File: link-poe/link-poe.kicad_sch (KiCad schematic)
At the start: 27 parts, among them J101 2x05_Horizontal, J102 NE8FAH, J103 JAE_DX07S016JA3, J104 2x05_Horizontal, J105 NE8FAH, J106 WAGO-2065, J107 WAGO-2065, J108 WAGO-2065, J109 WAGO-2065

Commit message: Refresh
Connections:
- net +24V-Supply renamed +24V-Link
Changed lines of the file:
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@@
 		)
 	)
-	(label "+24V-Supply"
+	(label "+24V-Link"
 		(at 78.74 52.07 180)
 		(effects
@@
 		)
 	)
-	(label "+24V-Supply"
+	(label "+24V-Link"
 		(at 46.99 26.67 0)
 		(effects
@@
 		)
 	)
-	(label "+24V-Supply"
+	(label "+24V-Link"
 		(at 78.74 90.17 180)
 		(effects
@@
 		)
 	)
-	(label "+24V-Supply"
+	(label "+24V-Link"
 		(at 30.48 158.75 0)
 		(effects

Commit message: Update
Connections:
- net Earth renamed USB-Shield
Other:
- note added: "PoE Passive +24V IEEE 802.3af Mode B"
- note added: "RS-422 3MHz"
- note added: "The cables used to connect the device and the power adapter reverse the order of the wires."
- note added: "V2 Link – PoE"
- note removed: "The cables connecting the device and the power adapter reverse the order of the wires. So these connectors are different from the otherwise identical connectors at the device."
- note removed: "V2 Link – PoE (Mode B)"
- title: V2 Link PoE (Mode B) -> V2 Link PoE
- moved on the sheet: C101, J101, J102, J103, J104, J105, J106, J107, J108, J109, R101, R102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

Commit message: Update usb + link-poe
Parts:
- C101: footprint Capacitor_SMD:C_0603_1608Metric -> V2_Capacitor_SMD:C_0603; symbol Device:C_Small -> V2_Device:C_0603_0u1; Mouser (none) -> 810-CGA3E2X7R1H104MA
- FID101, FID102, FID103: value Fiducial -> Fiducial_Paste
- ICON102: footprint V2_Artwork:Logo_Tiny -> V2_Artwork:Logo_Small
- INFO102: value ORDER-NUMBER -> Order_Number
- J101, J104: Mouser (none) -> 649-200211120001T4LF
- J102, J105: Mouser (none) -> 568-NE8FAH
- J103: value JAE_DX07S016JA3 -> DX07S016JA3; Mouser (none) -> 656-DX07S016JA3R1500
- J106, J107, J108, J109: value WAGO-2065 -> Conn_01x01
- R101, R102: footprint Resistor_SMD:R_0603_1608Metric -> V2_Resistor_SMD:R_0603; symbol Device:R_Small -> V2_Device:R_0603_5k1; Mouser (none) -> 71-CRCW06035K10FKEAC
- TVS101: value SMAJ36CA -> SMBJ36CA; footprint Diode_SMD:D_SMA -> V2_Diode_SMD:D_SMB; symbol V2_Diode:SMAJ36CA -> V2_Diode:SMBJ36CA; Mouser (none) -> 652-SMBJ36CA-Q
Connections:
- net USB-Shield renamed Earth

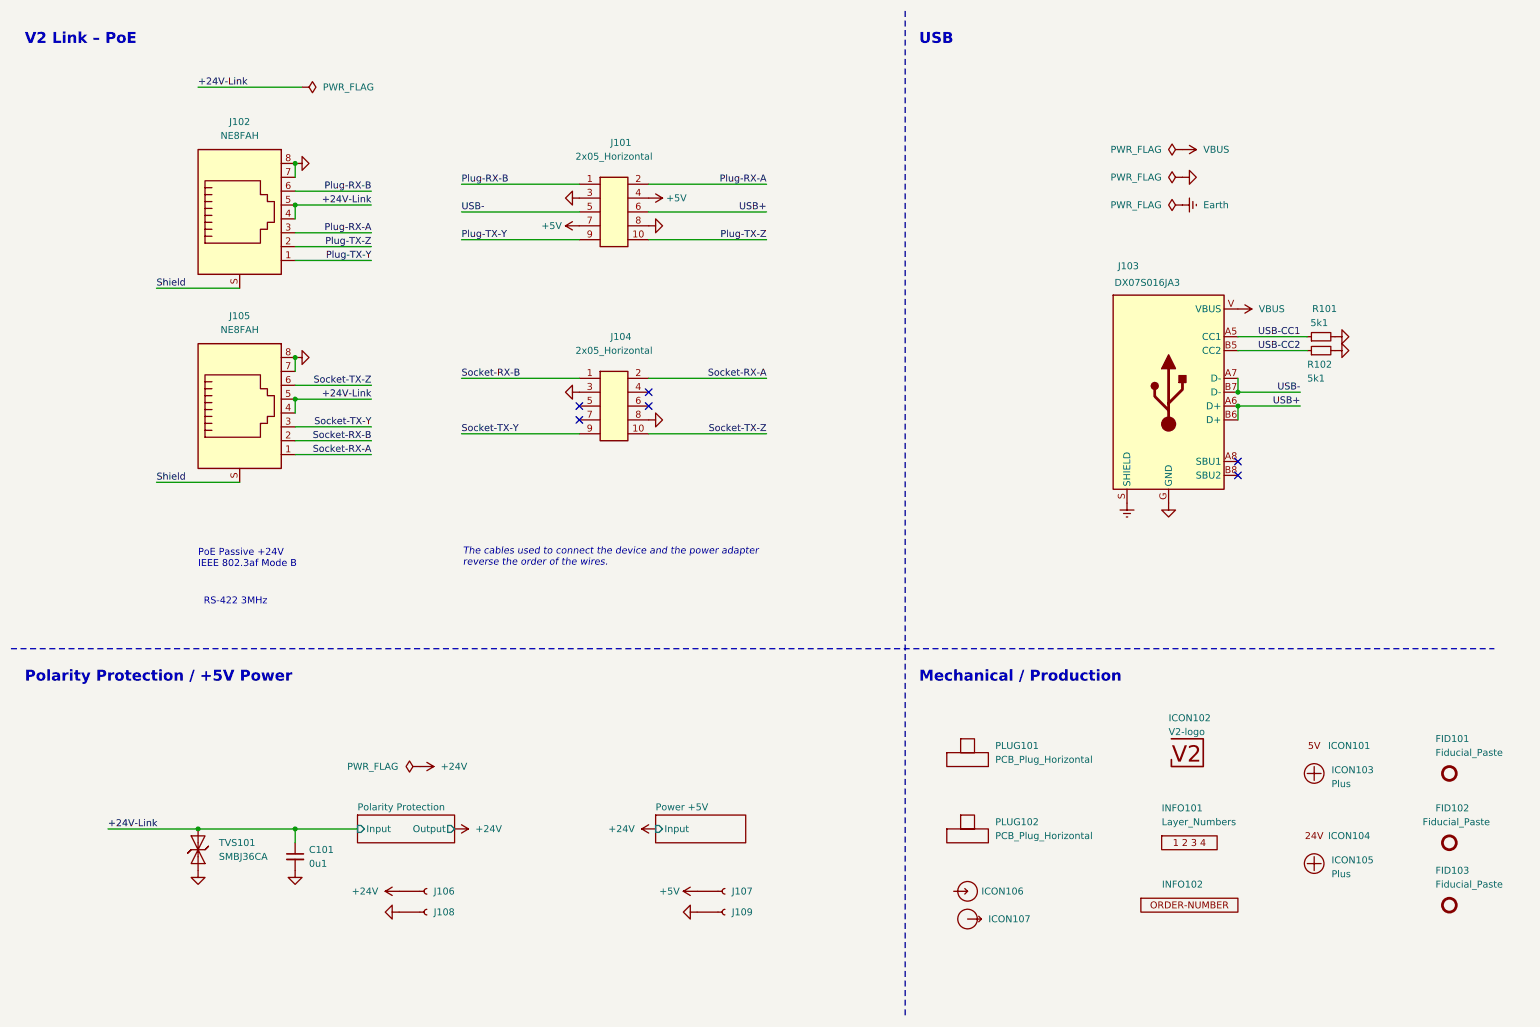
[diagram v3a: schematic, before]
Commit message: Update power symbols
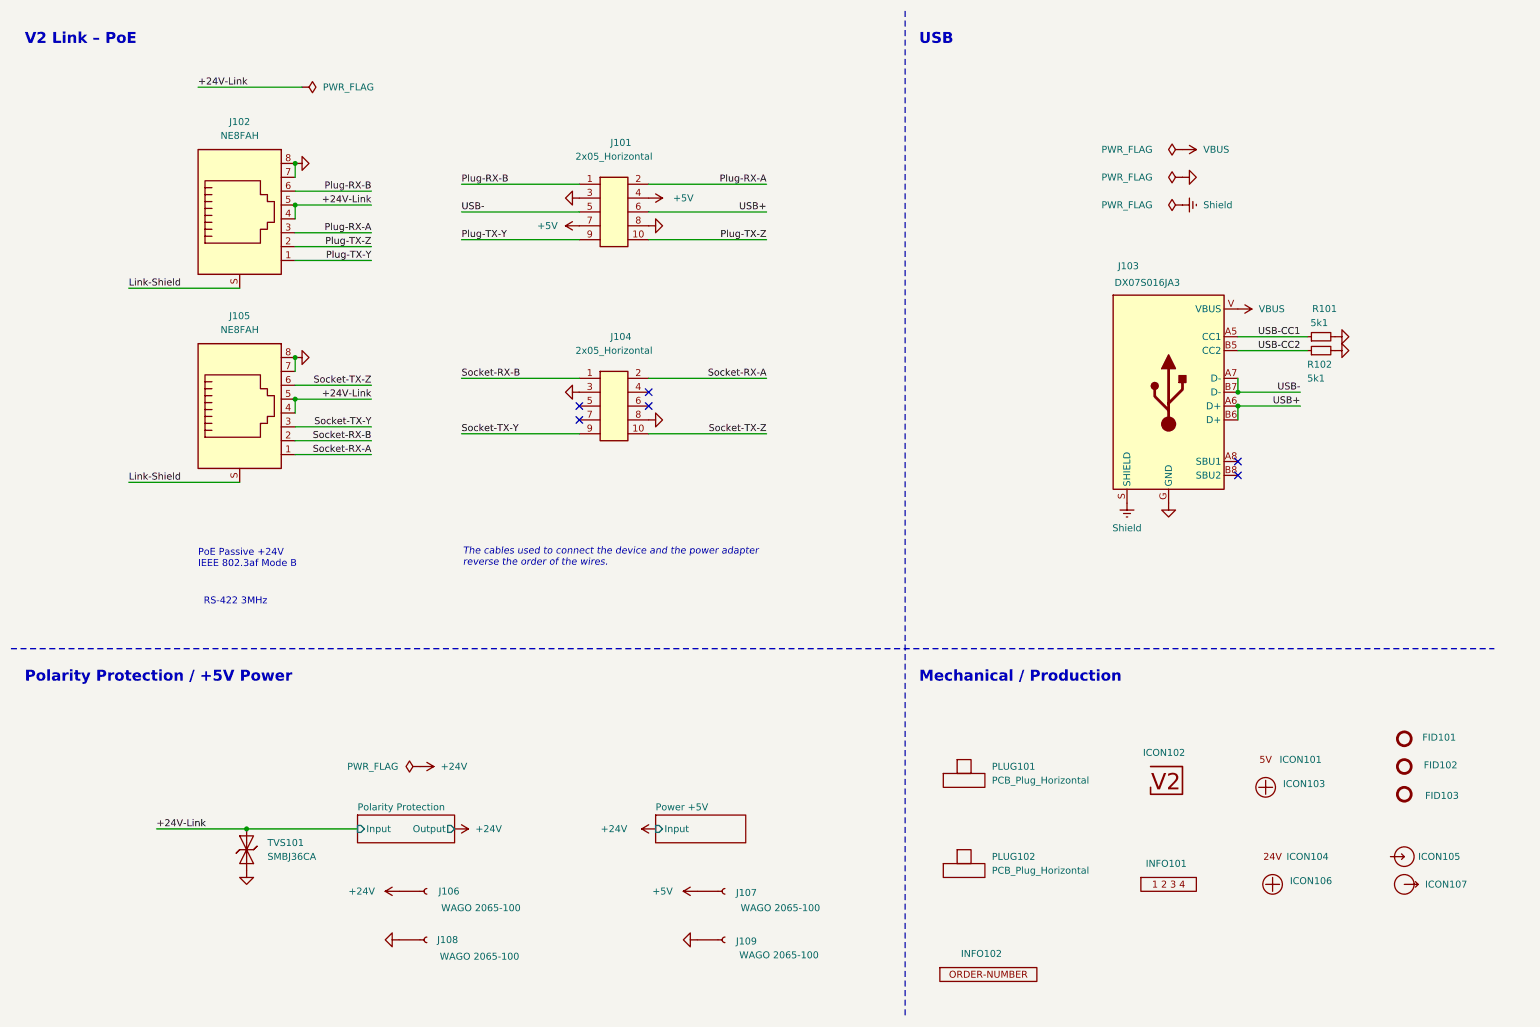
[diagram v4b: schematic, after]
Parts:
- removed C101: 0u1, V2_Capacitor_SMD:C_0603, symbol V2_Device:C_0603_0u1
- J106, J107, J108, J109: value Conn_01x01 -> WAGO 2065-100
- renumbered ICON106 to ICON105, ICON105 to ICON106
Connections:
- net Earth is gone; now on net Shield: J103.S (SHIELD)
- net Shield: no longer J102.S, J105.S
- new net Link-Shield: J102.S, J105.S
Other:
- moved on the sheet: FID101, FID102, FID103, ICON101, ICON102, ICON103, ICON104, ICON105, ICON106, ICON107, INFO101, INFO102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

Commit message: Refresh
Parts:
- J101, J104: Manufacturer (none) -> Amphenol FCI; Product (none) -> 20021112-00010T4LF
- J102, J105: Manufacturer (none) -> Neutrik; Product (none) -> NE8FAH
- J103: Manufacturer (none) -> JAE Electronics; Product (none) -> DX07S016JA3R1500
- J106, J107, J108, J109: Manufacturer (none) -> WAGO; Product (none) -> 2065-100/998-403
- R101, R102: Manufacturer (none) -> Vishay; Product (none) -> CRCW06035K10FKEAC; Rating (none) -> 100mW
- TVS101: Manufacturer (none) -> Bourns; Product (none) -> SMBJ36CA-Q; Rating (none) -> 36V

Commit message: Fix WAGOs
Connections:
- net +24V-Link renamed +VLINK
- net VBUS renamed +VBUS
